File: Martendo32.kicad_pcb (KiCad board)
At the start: 2 copper layers, 75.2 x 98.5 mm, 102 parts, among them CN2 ZX-MX1.25-2PWT, J1 AudioJack4_SwitchTR1, J2 Conn_01x03, J4 USB-C, Q1 NPN, Q2 AO3401A, SW1 SK-3296S-01-L3, U3 TP4056, U4 NS4168, U5 TPS61040DBV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

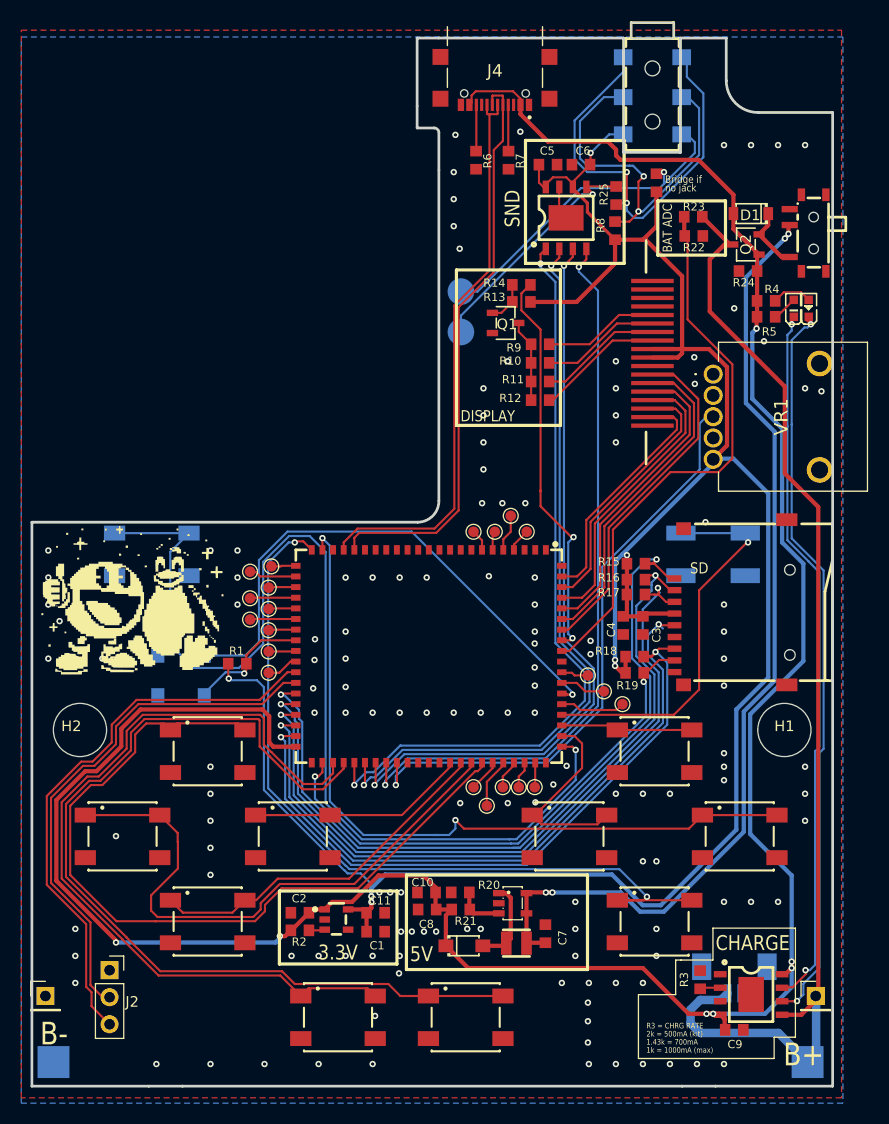
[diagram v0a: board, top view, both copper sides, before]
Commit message: Add files via upload
added Analog Joysticks RP1/RP1
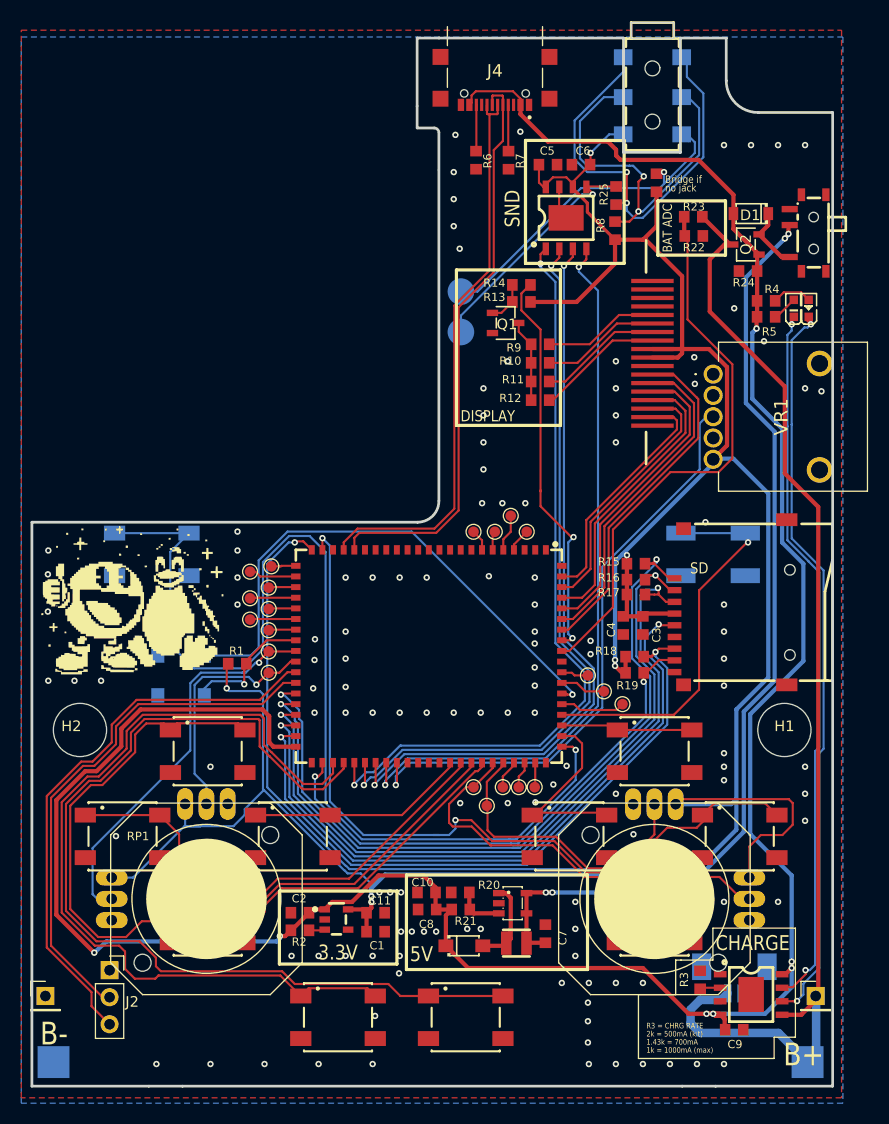
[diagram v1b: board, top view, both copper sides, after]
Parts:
- added RP1: Adafruit_2765, Martendo32Library:Adafruit_2765, F.Cu at (63.0, 134.0)
- added RP2: Adafruit_2765, Martendo32Library:Adafruit_2765, F.Cu at (105.1, 134.0)
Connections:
- net Net-(U1-ESP_LDO_VO4) renamed /RP1_X
- net Net-(U1-IO36) renamed /RP1_Y
- net Net-(U1-IO6) renamed /RP2_Y
- net Net-(U1-IO7) renamed /RP2_X
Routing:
- net /+3V3: track 225.0 -> 275.3 mm
- net /RP2_Y: track 3.05 -> 38.9 mm
- net /RP1_X: track 2.57 -> 36.9 mm, vias 0 -> 1
- net /RP2_X: track 4.69 -> 28.3 mm
- net /RP1_Y: track 2.98 -> 22.7 mm, vias 0 -> 1
- net /KEY_RIGHT2: track 72.0 -> 76.7 mm
- net /KEY_UP1: track 75.1 -> 78.2 mm
- net /KEY_SELECT1: track 77.2 -> 80.3 mm
- net +5V: track 240.0 -> 242.4 mm
- net /KEY_START1: track 88.5 -> 90.8 mm
- net /BOOT: track 11.5 -> 13.3 mm
- net /SD_CMD: track 69.1 -> 69.7 mm
- net /KEY_LEFT2: track 18.7 -> 18.2 mm
- net /SD_DAT2: track 73.7 -> 73.1 mm
- net GND: vias 139 -> 132

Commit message: Add files via upload
improved Silkscreen
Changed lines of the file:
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@@
 		(at 62.99 133.978 180)
 		(property "Reference" "RP1"
-			(at 6.428 5.882 0)
+			(at -0.126 5.882 0)
 			(unlocked yes)
 			(layer "F.SilkS")
+			(hide yes)
 			(effects
 				(font
@@
 		(sheetfile "Martendo32.kicad_sch")
 		(attr smd dnp)
-		(fp_line
-			(start 9 6)
-			(end 6 9)
-			(stroke
-				(width 0.127)
-				(type solid)
-			)
-			(layer "F.SilkS")
-		)
-		(fp_line
-			(start 9 -6)
-			(end 9 6)
-			(stroke
-				(width 0.127)
-				(type solid)
-			)
-			(layer "F.SilkS")
-		)
-		(fp_line
-			(start 6 9)
-			(end -6 9)
-			(stroke
-				(width 0.127)
-				(type solid)
-			)
-			(layer "F.SilkS")
-		)
-		(fp_line
-			(start 6 -9)
-			(end 9 -6)
-			(stroke
-				(width 0.127)
-				(type solid)
-			)
-			(layer "F.SilkS")
-		)
-		(fp_line
-			(start -6 9)
-			(end -9 6)
-			(stroke
-				(width 0.127)
-				(type solid)
-			)
-			(layer "F.SilkS")
-		)
-		(fp_line
-			(start -6 -9)
-			(end 6 -9)
-			(stroke
-				(width 0.127)
-				(type solid)
-			)
-			(layer "F.SilkS")
-		)
-		(fp_line
-			(start -9 6)
-			(end -9 -6)
-			(stroke
-				(width 0.127)
-				(type solid)
-			)
-			(layer "F.SilkS")
-		)
-		(fp_line
-			(start -9 -6)
-			(end -6 -9)
-			(stroke
-				(width 0.127)
-				(type solid)
-			)
-			(layer "F.SilkS")
-		)
-		(fp_circle
-			(center 0 0)
-			(end 0 7)
-			(stroke
-				(width 0.127)
-				(type solid)
-			)
-			(fill no)
-			(layer "F.SilkS")
-		)
-		(fp_poly
-			(pts
-				(xy 5.64421 0.467692) (xy 5.58631 0.932191) (xy 5.490251 1.390321) (xy 5.356688 1.838953) (xy 5.186532 2.275024)
-				(xy 4.980947 2.695554) (xy 4.741338 3.097671) (xy 4.46934 3.478627) (xy 4.166812 3.835821) (xy 3.835821 4.166812)
-				(xy 3.478627 4.46934) (xy 3.097671 4.741338) (xy 2.695554 4.980947) (xy 2.275024 5.186532) (xy 1.838953 5.356688)
-				(xy 1.390321 5.490251) (xy 0.930903 5.586581) (xy 0.001315 5.663609) (xy -0.467692 5.64421) (xy -0.932191 5.58631)
-				(xy -1.390321 5.490251) (xy -1.838953 5.356688) (xy -2.275024 5.186532) (xy -2.695554 4.980947)
-				(xy -3.097671 4.741338) (xy -3.478627 4.46934) (xy -3.835821 4.166812) (xy -4.166812 3.835821) (xy -4.46934 3.478627)
-				(xy -4.741338 3.097671) (xy -4.980947 2.695554) (xy -5.186532 2.275024) (xy -5.356688 1.838953)
-				(xy -5.490251 1.390321) (xy -5.58631 0.932191) (xy -5.64421 0.467692) (xy -5.663554 0) (xy -5.64421 -0.467692)
-				(xy -5.58631 -0.932191) (xy -5.490251 -1.390321) (xy -5.356688 -1.838953) (xy -5.186532 -2.275024)
-				(xy -4.980947 -2.695554) (xy -4.741338 -3.097671) (xy -4.46934 -3.478627) (xy -4.166812 -3.835821)
-				(xy -3.835821 -4.166812) (xy -3.478627 -4.46934) (xy -3.097671 -4.741338) (xy -2.695554 -4.980947)
-				(xy -2.275024 -5.186532) (xy -1.838953 -5.356688) (xy -1.390321 -5.490251) (xy -0.932191 -5.58631)
-				(xy -0.467692 -5.64421) (xy 0 -5.663554) (xy 0.467692 -5.64421) (xy 0.932191 -5.58631) (xy 1.390321 -5.490251)
-				(xy 1.838953 -5.356688) (xy 2.275024 -5.186532) (xy 2.695554 -4.980947) (xy 3.097671 -4.741338)
-				(xy 3.478627 -4.46934) (xy 3.835821 -4.166812) (xy 4.166812 -3.835821) (xy 4.46934 -3.478627) (xy 4.741338 -3.097671)
-				(xy 4.980947 -2.695554) (xy 5.186532 -2.275024) (xy 5.356688 -1.838953) (xy 5.490251 -1.390321)
-				(xy 5.58631 -0.932191) (xy 5.64421 -0.467692) (xy 5.663554 0)
-			)
-			(stroke
-				(width 0)
-				(type default)
-			)
-			(fill yes)
-			(layer "F.SilkS")
-		)
 		(pad "" np_thru_hole circle
 			(at -6 6 90)
@@
 		(at 105.09 133.978 90)
 		(property "Reference" "RP2"
-			(at 6.428 5.882 270)
+			(at 5.562 2.222 0)
 			(unlocked yes)
 			(layer "F.SilkS")
@@
 		(sheetfile "Martendo32.kicad_sch")
 		(attr smd dnp)
-		(fp_line
-			(start 6 -9)
-			(end 9 -6)
-			(stroke
-				(width 0.127)
-				(type solid)
-			)
-			(layer "F.SilkS")
-		)
-		(fp_line
-			(start -6 -9)
-			(end 6 -9)
-			(stroke
-				(width 0.127)
-				(type solid)
-			)
-			(layer "F.SilkS")
-		)
-		(fp_line
-			(start 9 -6)
-			(end 9 6)
-			(stroke
-				(width 0.127)
-				(type solid)
-			)
-			(layer "F.SilkS")
-		)
-		(fp_line
-			(start -9 -6)
-			(end -6 -9)
-			(stroke
-				(width 0.127)
-				(type solid)
-			)
-			(layer "F.SilkS")
-		)
-		(fp_line
-			(start 9 6)
-			(end 6 9)
-			(stroke
-				(width 0.127)
-				(type solid)
-			)
-			(layer "F.SilkS")
-		)
-		(fp_line
-			(start -9 6)
-			(end -9 -6)
-			(stroke
-				(width 0.127)
-				(type solid)
-			)
-			(layer "F.SilkS")
-		)
-		(fp_line
-			(start 6 9)
-			(end -6 9)
-			(stroke
-				(width 0.127)
-				(type solid)
-			)
-			(layer "F.SilkS")
-		)
-		(fp_line
-			(start -6 9)
-			(end -9 6)
-			(stroke
-				(width 0.127)
-				(type solid)
-			)
-			(layer "F.SilkS")
-		)
-		(fp_circle
-			(center 0 0)
-			(end 0 7)
-			(stroke
-				(width 0.127)
-				(type solid)
-			)
-			(fill no)
-			(layer "F.SilkS")
-		)
-		(fp_poly
-			(pts
-				(xy 5.64421 0.467692) (xy 5.58631 0.932191) (xy 5.490251 1.390321) (xy 5.356688 1.838953) (xy 5.186532 2.275024)
-				(xy 4.980947 2.695554) (xy 4.741338 3.097671) (xy 4.46934 3.478627) (xy 4.166812 3.835821) (xy 3.835821 4.166812)
-				(xy 3.478627 4.46934) (xy 3.097671 4.741338) (xy 2.695554 4.980947) (xy 2.275024 5.186532) (xy 1.838953 5.356688)
-				(xy 1.390321 5.490251) (xy 0.930903 5.586581) (xy 0.001315 5.663609) (xy -0.467692 5.64421) (xy -0.932191 5.58631)
-				(xy -1.390321 5.490251) (xy -1.838953 5.356688) (xy -2.275024 5.186532) (xy -2.695554 4.980947)
-				(xy -3.097671 4.741338) (xy -3.478627 4.46934) (xy -3.835821 4.166812) (xy -4.166812 3.835821) (xy -4.46934 3.478627)
-				(xy -4.741338 3.097671) (xy -4.980947 2.695554) (xy -5.186532 2.275024) (xy -5.356688 1.838953)
-				(xy -5.490251 1.390321) (xy -5.58631 0.932191) (xy -5.64421 0.467692) (xy -5.663554 0) (xy -5.64421 -0.467692)
-				(xy -5.58631 -0.932191) (xy -5.490251 -1.390321) (xy -5.356688 -1.838953) (xy -5.186532 -2.275024)
-				(xy -4.980947 -2.695554) (xy -4.741338 -3.097671) (xy -4.46934 -3.478627) (xy -4.166812 -3.835821)
-				(xy -3.835821 -4.166812) (xy -3.478627 -4.46934) (xy -3.097671 -4.741338) (xy -2.695554 -4.980947)
-				(xy -2.275024 -5.186532) (xy -1.838953 -5.356688) (xy -1.390321 -5.490251) (xy -0.932191 -5.58631)
-				(xy -0.467692 -5.64421) (xy 0 -5.663554) (xy 0.467692 -5.64421) (xy 0.932191 -5.58631) (xy 1.390321 -5.490251)
-				(xy 1.838953 -5.356688) (xy 2.275024 -5.186532) (xy 2.695554 -4.980947) (xy 3.097671 -4.741338)
-				(xy 3.478627 -4.46934) (xy 3.835821 -4.166812) (xy 4.166812 -3.835821) (xy 4.46934 -3.478627) (xy 4.741338 -3.097671)
-				(xy 4.980947 -2.695554) (xy 5.186532 -2.275024) (xy 5.356688 -1.838953) (xy 5.490251 -1.390321)
-				(xy 5.58631 -0.932191) (xy 5.64421 -0.467692) (xy 5.663554 0)
-			)
-			(stroke
-				(width 0)
-				(type default)
-			)
-			(fill yes)
-			(layer "F.SilkS")
-		)
 		(pad "" np_thru_hole circle
 			(at -6 6)

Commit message: Add files via upload
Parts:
- added R26: 10K, Resistor_SMD:R_0603_1608Metric_Pad0.98x0.95mm_HandSolder, F.Cu at (88.2, 82.7)
- added TP22: TestPoint, TestPoint:TestPoint_Pad_D1.0mm, F.Cu at (86.1, 99.5)
- added TP23: TestPoint, TestPoint:TestPoint_Pad_D1.0mm, F.Cu at (86.1, 97.5)
- moved CN2 4.25 mm to (111.6, 145.7)
- moved R13 2.65 mm to (89.9, 77.9)
- moved R14 2.65 mm to (89.9, 76.3)
- moved Q1 2.65 mm to (88.5, 79.9)
- moved R10 2.65 mm to (91.7, 83.6)
- moved R11 2.65 mm to (91.7, 85.4)
- moved R12 2.65 mm to (91.7, 87.1)
- moved R9 2.65 mm to (91.7, 81.9)
- moved TP4 1.82 mm to (88.8, 123.5), turned to 0 degrees
- moved J2 1.67 mm to (52.6, 141.7)
- moved TP5 1.60 mm to (87.1, 124.7), turned to 0 degrees
- moved TP18 0.35 mm to (69.1, 111.0)
- moved TP21 0.35 mm to (69.1, 113.0)
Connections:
- net Net-(U1-IO28) renamed /LCD_BACK_ALT
- RP2 pad Y: /RP2_Y -> /LCD_BACK
- TP18 pad 1: /RP1_X -> Net-(U1-ESP_LDO_VO4)
- TP21 pad 1: /RP1_Y -> Net-(U1-IO36)
- TP4 pad 1: /RP2_X -> Net-(U1-IO7)
- TP5 pad 1: /RP2_Y -> Net-(U1-IO6)
- U1 pad 16: unconnected-(U1-USB_DM-Pad16) -> Net-(U1-USB_DM)
- U1 pad 17: unconnected-(U1-USB_DP-Pad17) -> Net-(U1-USB_DP)
- U1 pad 32: /RP1_X -> Net-(U1-ESP_LDO_VO4)
- U1 pad 33: /RP1_Y -> Net-(U1-IO36)
- U1 pad 51: /KEY_FN1 -> /RP1_X
- U1 pad 52: /KEY_L -> /RP1_Y
- U1 pad 54: /KEY_R -> /RP2_X
- U1 pad 59: /RP2_Y -> Net-(U1-IO6)
- U1 pad 60: /RP2_X -> Net-(U1-IO7)
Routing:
- net /LCD_BACK: track 37.3 -> 99.2 mm, vias 2 -> 3
- net /RP2_Y: track 38.9 -> 0.00 mm
- net /LCD_BACK_ALT: track 2.32 -> 38.6 mm, vias 0 -> 2
- net /CHIP_PU: track 51.8 -> 66.8 mm
- net /RP1_X: track 36.9 -> 51.7 mm, vias 1 -> 0
- net Net-(U1-USB_DP): track 0.00 -> 13.5 mm, vias 0 -> 2
- net Net-(U1-USB_DM): track 0.00 -> 12.0 mm, vias 0 -> 2
- net /BAT+: track 108.9 -> 101.1 mm
- net /RP1_Y: track 22.7 -> 30.0 mm, vias 1 -> 0
- net Net-(U1-IO6): track 0.00 -> 5.16 mm
- net /+3V3: track 275.3 -> 280.1 mm
- net Net-(Q1-B): track 3.89 -> 8.42 mm
- net /RP2_X: track 28.3 -> 31.9 mm, vias 0 -> 2
- net Net-(U1-IO7): track 0.00 -> 3.30 mm
- net Net-(U1-IO36): track 0.00 -> 2.84 mm
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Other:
- outline, holes or cut-outs redrawn
- board text added: "BOOT"
- board text added: "Enable P4 chip"
